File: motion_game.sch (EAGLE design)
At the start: 4 parts

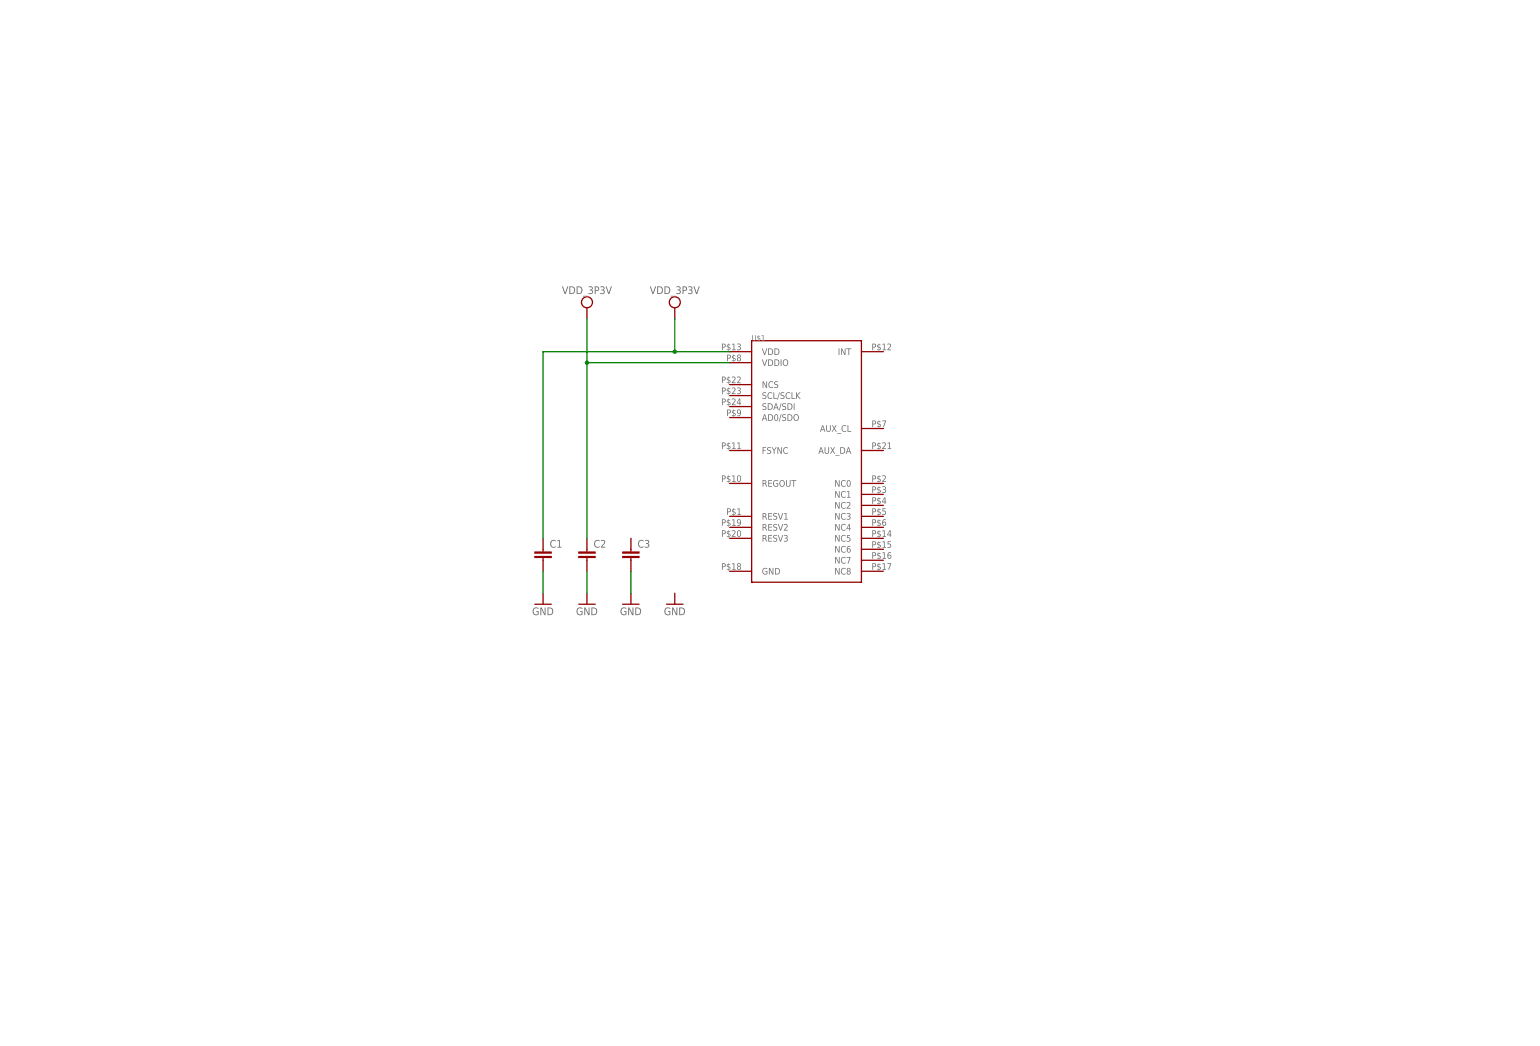
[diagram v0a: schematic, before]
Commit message: route pdb
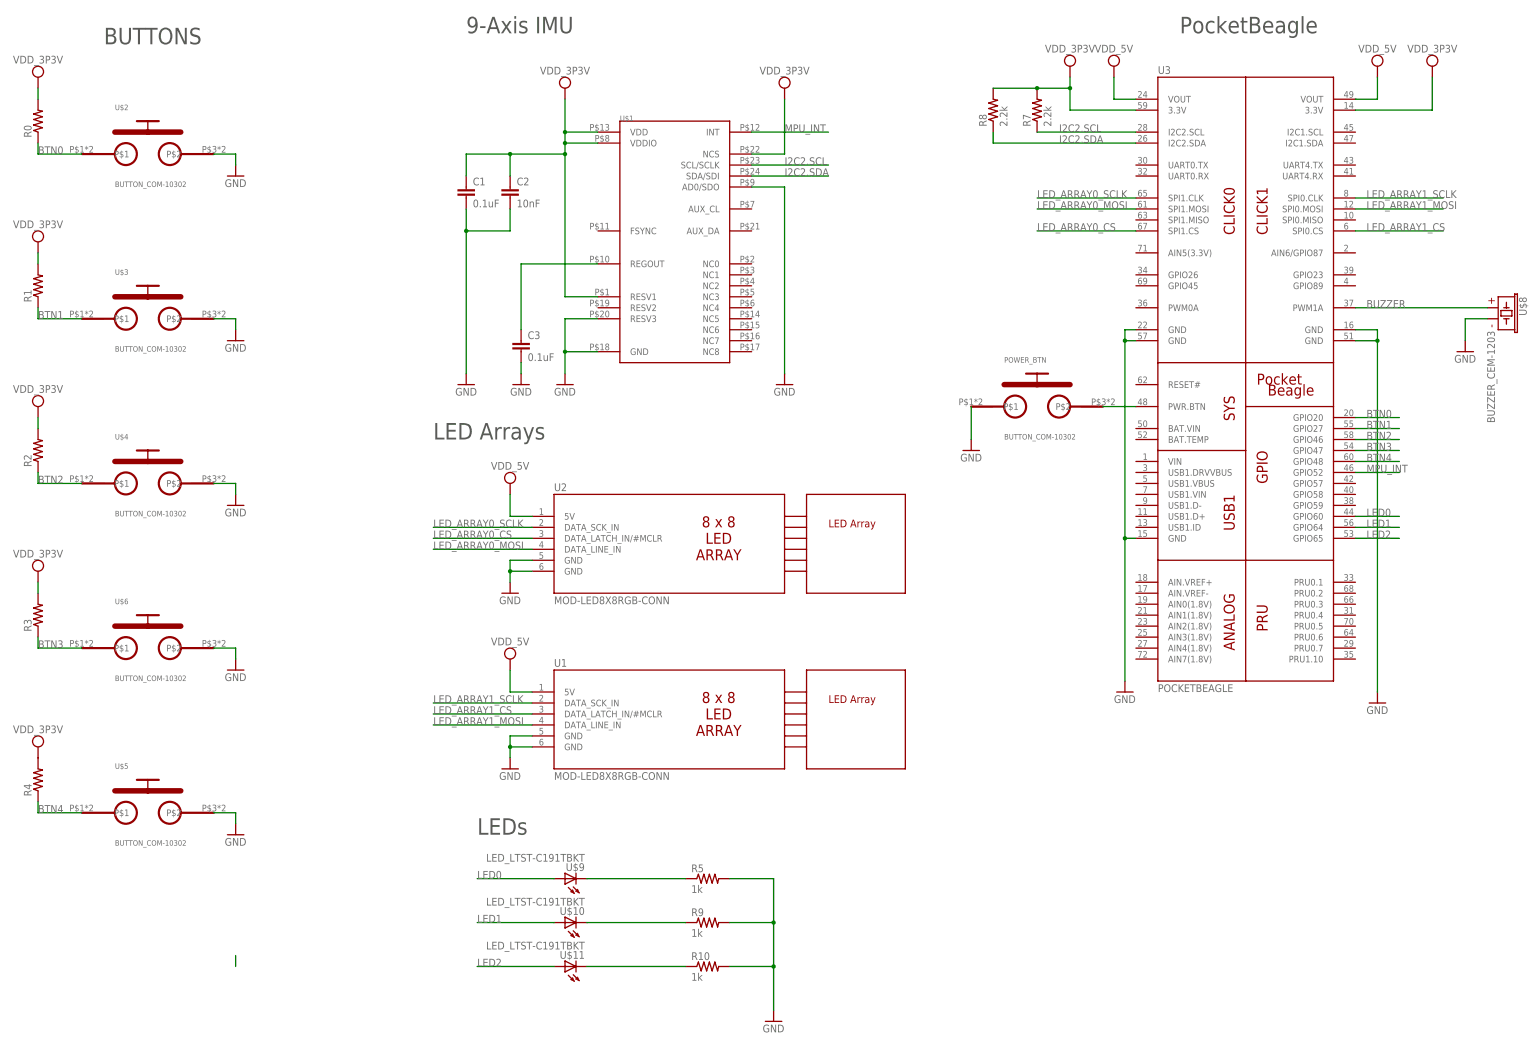
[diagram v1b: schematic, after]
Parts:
- added POWER_BTN, U$2, U$3, U$4, U$5, U$6: BUTTON_COM-10302, motion_game:BUTTON_COM-10302
- added R0, R1, R2, R3, R4: (no value), motion_game:R_R0603
- added R10, R5, R9: 1k, Maze_game:R_R0603
- added R7, R8: 2.2k, motion_game:R_R0603
- added U$10, U$11, U$9: LED_LTST-C191TBKT, motion_game:LED_LTST-C191TBKT
- added U$12, U$7: MOD-LED8X8RGB-OUTLINE, Maze_game:MOD-LED8X8RGB-OUTLINE
- added U$8: BUZZER_CEM-1203, Maze_game:BUZZER_CEM-1203
- added U1, U2: MOD-LED8X8RGB-CONN, ENGI301_Maze_Project_Parts:MOD-LED8X8RGB-CONN
- added U3: POCKETBEAGLE, motion_game:POCKETBEAGLE
- C1, C3: value (none) -> 0.1uF
- C2: value (none) -> 10nF
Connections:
- new net BTN0: R0.1, U$2.P$1, U3.GPIO20
- new net BTN1: R1.1, U$3.P$1, U3.GPIO27
- new net BTN2: R2.1, U$4.P$1, U3.GPIO46
- new net BTN3: R3.1, U$6.P$1, U3.GPIO47
- new net BTN4: R4.1, U$5.P$1, U3.GPIO48
- new net BUZZER: U$8.1, U3.PWM1A
- new net I2C2.SCL: R7.1, U$1.SCL/SCLK, U3.I2C2.SCL
- new net I2C2.SDA: R8.1, U$1.SDA/SDI, U3.I2C2.SDA
- new net LED0: U$9.A, U3.GPIO60
- new net LED1: U$10.A, U3.GPIO64
- new net LED2: U$11.A, U3.GPIO65
- new net LED_ARRAY0_CS: U2.DATA_LATCH_IN/#MCLR, U3.SPI1.CS
- new net LED_ARRAY0_MOSI: U2.DATA_LINE_IN, U3.SPI1.MOSI
- new net LED_ARRAY0_SCLK: U2.DATA_SCK_IN, U3.SPI1.CLK
- new net LED_ARRAY1_CS: U1.DATA_LATCH_IN/#MCLR, U3.SPI0.CS
- new net LED_ARRAY1_MOSI: U1.DATA_LINE_IN, U3.SPI0.MOSI
- new net LED_ARRAY1_SCLK: U1.DATA_SCK_IN, U3.SPI0.CLK
- new net MPU_INT: U$1.INT, U3.GPIO52
- new net N$10: POWER_BTN.P$2, U3.PWR.BTN
- new net N$13: C3.1, U$1.REGOUT
- new net N$36: R9.1, U$10.C
- new net N$37: R10.1, U$11.C
- new net N$6: R5.1, U$9.C
- net GND: now also POWER_BTN.P$1, R10.2, R5.2, R9.2, U$1.AD0/SDO, U$1.GND, U$1.RESV3, U$2.P$2, U$3.P$2, U$4.P$2, U$5.P$2, U$6.P$2, U$8.2, U1.GND@1, U1.GND@2, U2.GND@1, U2.GND@2, U3.GND@1, U3.GND@2, U3.GND@3, U3.GND@4, U3.GND@5
- net SYS_VDD1_3P3V: now also R0.2, R1.2, R2.2, R3.2, R4.2, R7.2, R8.2, U$1.NCS, U$1.RESV1, U1.5V, U2.5V, U3.3.3V@1, U3.3.3V@2, U3.VOUT@1, U3.VOUT@2
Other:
- note added: "9-Axis IMU"
- note added: "BUTTONS"
- note added: "LED Arrays"
- note added: "LEDs"
- note added: "PocketBeagle"
- moved on the sheet: C1, C2, C3, U$1

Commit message: adjust Vdd
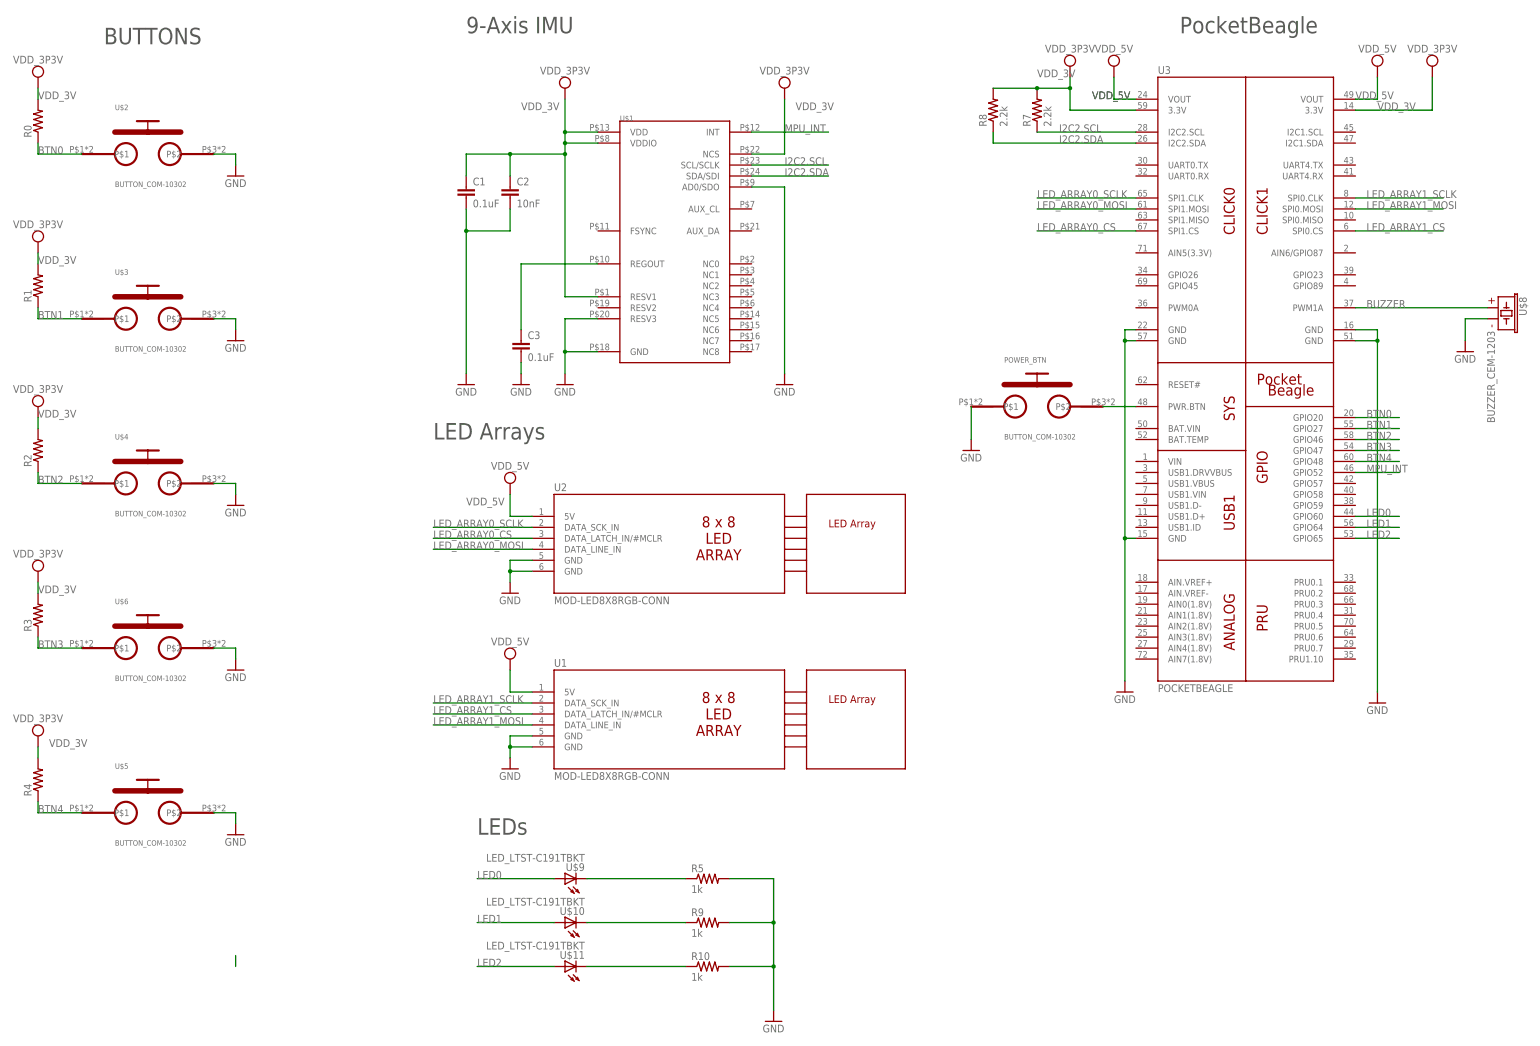
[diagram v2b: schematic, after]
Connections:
- removed net SYS_VDD1_3P3V: C1.1, C2.1, R0.2, R1.2, R2.2, R3.2, R4.2, R7.2, R8.2, U$1.NCS, U$1.RESV1, U$1.VDD, U$1.VDDIO, U1.5V, U2.5V, U3.3.3V@1, U3.3.3V@2, U3.VOUT@1, U3.VOUT@2
- new net VDD_3V: C1.1, C2.1, R0.2, R1.2, R2.2, R3.2, R4.2, R7.2, R8.2, U$1.NCS, U$1.RESV1, U$1.VDD, U$1.VDDIO, U3.3.3V@1, U3.3.3V@2
- new net VDD_5V: U1.5V, U2.5V, U3.VOUT@1, U3.VOUT@2
